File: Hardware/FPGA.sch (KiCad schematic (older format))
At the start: 13 parts, among them U501 W25Q128JVxxM, U502 ICE40UP5K-SG48, U503 Crystal Oscillator, U504 USBLC6-2

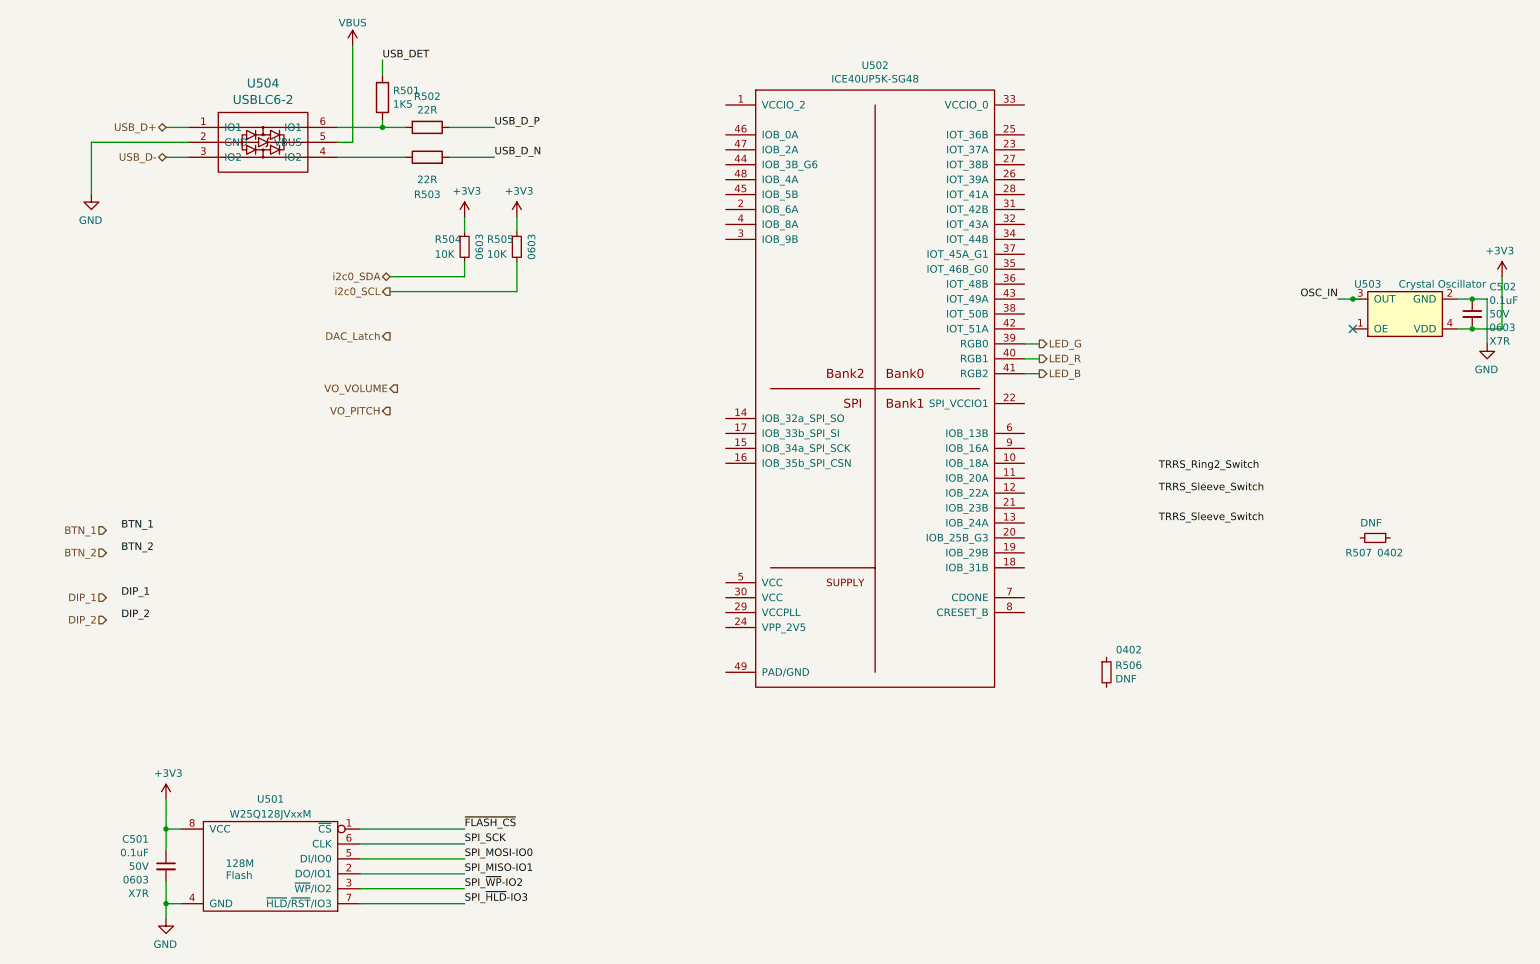
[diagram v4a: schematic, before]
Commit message: Hooking up switches, some more connectivity.
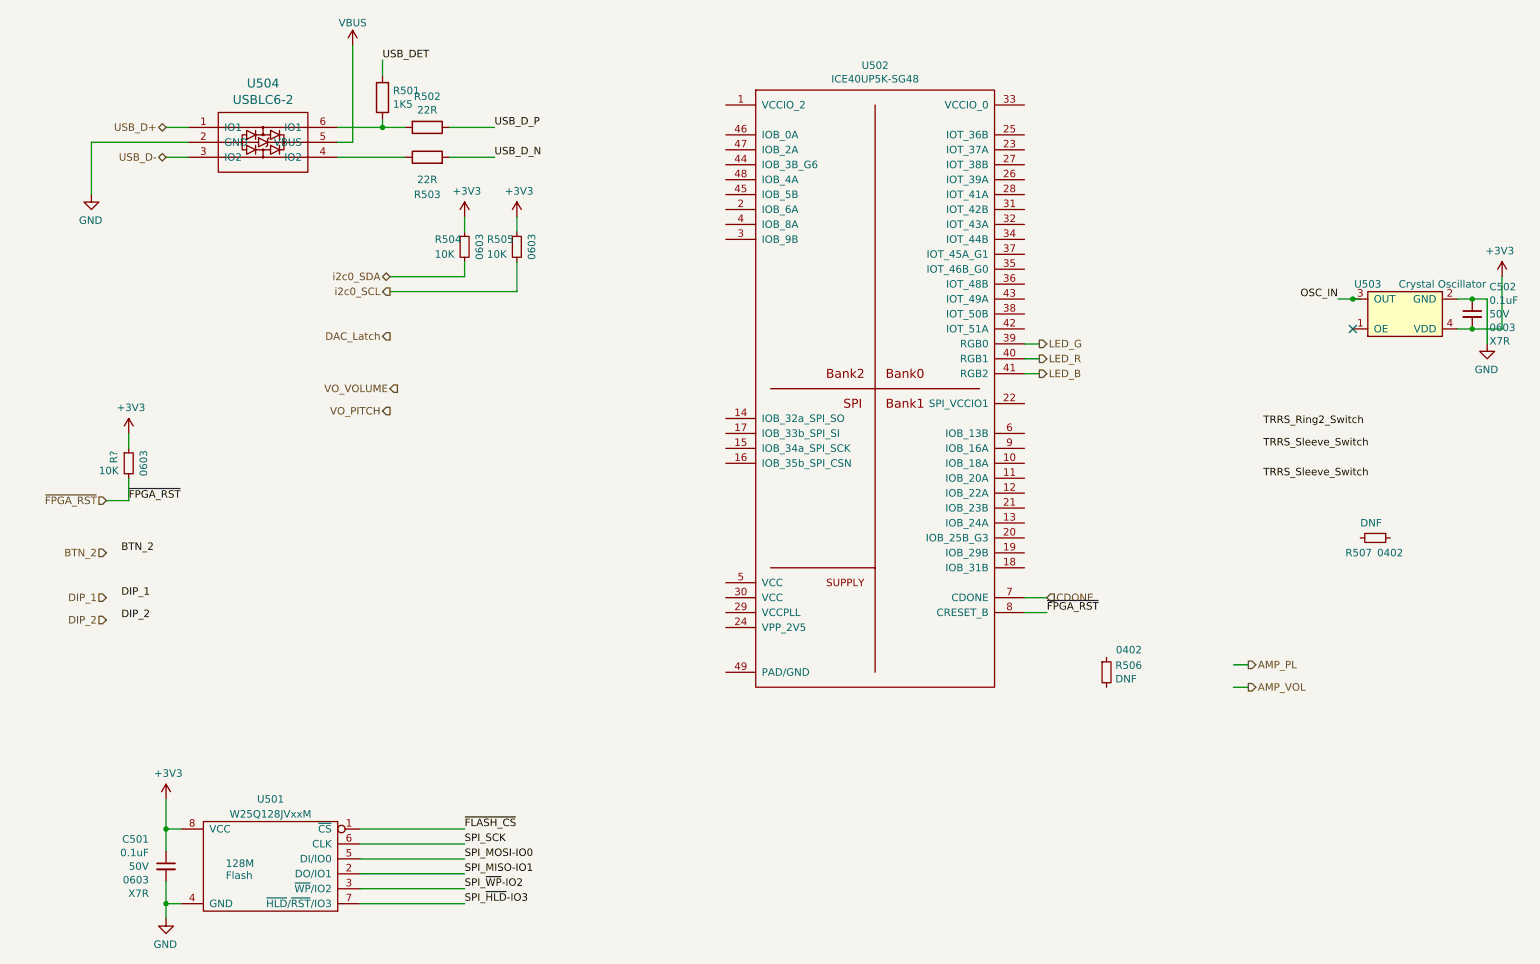
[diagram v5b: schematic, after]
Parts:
- added R?: 10K, Resistor_SMD:R_0603_1608Metric, symbol Device:R_Small
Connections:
- net labels added: AMP_PL, AMP_VOL, CDONE, ~FPGA_RST
- net labels removed: BTN_1
- wire segments 42 -> 49
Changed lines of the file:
@@
 Text HLabel 1300 4250 0    50   Input ~ 0
 BTN_2
-Text HLabel 1300 4100 0    50   Input ~ 0
-BTN_1
+Text HLabel 1300 3900 0    50   Input ~ 0
+~FPGA_RST
 Text HLabel 1300 4700 0    50   Input ~ 0
 DIP_2
@@
 Text Label 1400 4700 0    50   ~ 0
 DIP_2
-Text Label 1400 4100 0    50   ~ 0
-BTN_1
 Text Label 1400 4250 0    50   ~ 0
 BTN_2
@@
 	0    1    1    0
 $EndComp
-Text Label 8350 3700 0    50   ~ 0
+Text Label 9050 3400 0    50   ~ 0
 TRRS_Ring2_Switch
-Text Label 8350 3850 0    50   ~ 0
+Text Label 9050 3550 0    50   ~ 0
 TRRS_Sleeve_Switch
-Text Label 8350 4050 0    50   ~ 0
+Text Label 9050 3750 0    50   ~ 0
 TRRS_Sleeve_Switch
+Text HLabel 8950 5150 2    50   Output ~ 0
+AMP_VOL
+Wire Wire Line
+	8950 5150 8850 5150
+Text HLabel 8950 5000 2    50   Output ~ 0
+AMP_PL
+Wire Wire Line
+	8950 5000 8850 5000
+$Comp
+L Device:R_Small R?
+U 1 1 6165C82A
+P 1450 3650
+AR Path="/611E335F/6165C82A" Ref="R?"  Part="1"
+AR Path="/6165C82A" Ref="R?"  Part="1"
+AR Path="/611E3335/6165C82A" Ref="R?"  Part="1"
+F 0 "R?" V 1350 3650 50  0000 L CNN
+F 1 "10K" H 1250 3600 50  0000 L CNN
+F 2 "Resistor_SMD:R_0603_1608Metric" V 1380 3650 50  0001 C CNN
+F 3 "~" H 1450 3650 50  0001 C CNN
+F 4 "0603" V 1550 3650 50  0000 C CNN "Pkg"
+F 5 "RNCP0603FTD10K0" H 1450 3650 50  0001 C CNN "MPN"
+F 6 "RNCP0603FTD10K0CT-ND" H 1450 3650 50  0001 C CNN "DPN"
+	1    1450 3650
+	1    0    0    -1
+$EndComp
+Wire Wire Line
+	1450 3750 1450 3900
+$Comp
+L power:+3V3 #PWR?
+U 1 1 6165C831
+P 1450 3450
+AR Path="/611E3335/6165C831" Ref="#PWR?"  Part="1"
+AR Path="/6165C831" Ref="#PWR?"  Part="1"
+F 0 "#PWR?" H 1450 3300 50  0001 C CNN
+F 1 "+3V3" H 1465 3623 50  0000 C CNN
+F 2 "" H 1450 3450 50  0001 C CNN
+F 3 "" H 1450 3450 50  0001 C CNN
+	1    1450 3450
+	1    0    0    -1
+$EndComp
+Wire Wire Line
+	1450 3450 1450 3550
+Wire Wire Line
+	1300 3900 1450 3900
+Text Label 1450 3900 0    50   ~ 0
+~FPGA_RST
+Text Label 7600 4650 0    50   ~ 0
+~FPGA_RST
+Wire Wire Line
+	7450 4650 7600 4650
+Text HLabel 7600 4550 2    50   Input ~ 0
+CDONE
+Wire Wire Line
+	7600 4550 7450 4550
 $EndSCHEMATC

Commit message: FPGA wiring.
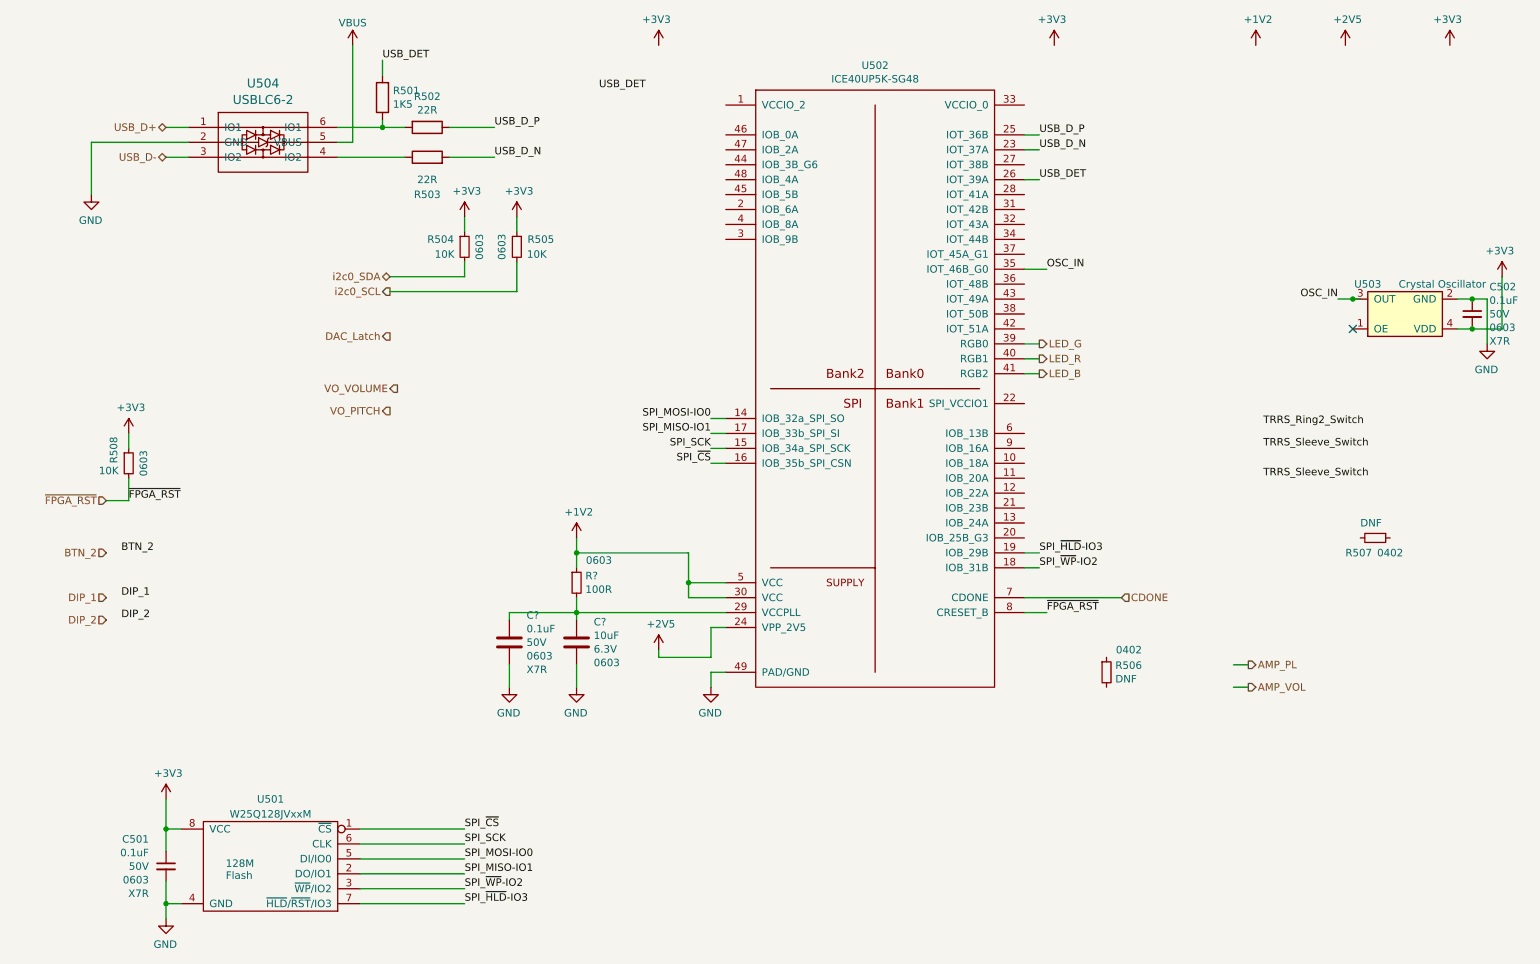
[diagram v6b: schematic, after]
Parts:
- added C?: 10uF, Capacitor_SMD:C_0603_1608Metric, symbol Device:C
- added C?: 0.1uF, Capacitor_SMD:C_0603_1608Metric, symbol Device:C
- added R?: 100R, Resistor_SMD:R_0603_1608Metric, symbol Device:R_Small
- gave numbers to parts that had none: 1
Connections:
- net labels added: +1V2, +2V5, SPI_~CS
- net labels removed: ~FLASH_CS
- wire segments 49 -> 79

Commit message: Wiring up FPGA, picking pins.
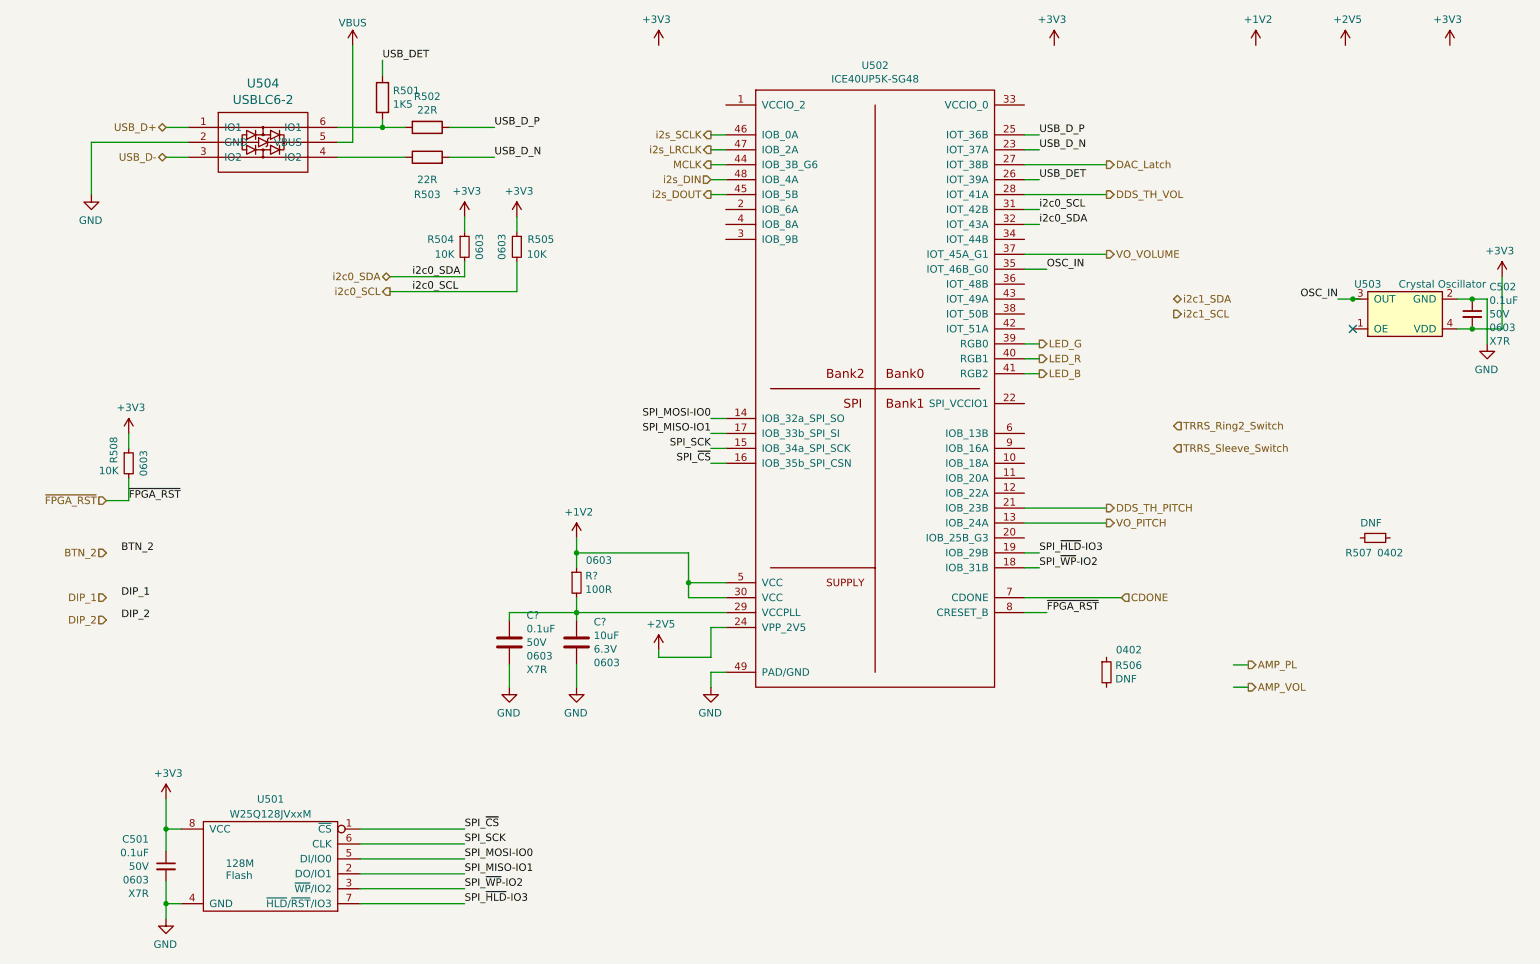
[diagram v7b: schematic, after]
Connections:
- net labels added: DDS_TH_PITCH, DDS_TH_VOL, MCLK, i2c1_SCL, i2c1_SDA, i2s_DIN, i2s_DOUT, i2s_LRCLK, i2s_SCLK
- wire segments 79 -> 91
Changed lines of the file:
@@
 Text HLabel 3200 2500 0    50   Output ~ 0
 i2c0_SCL
-Text HLabel 3200 2800 0    50   Output ~ 0
+Text HLabel 8000 1650 2    50   Output ~ 0
 DAC_Latch
-Text HLabel 3250 3150 0    50   Output ~ 0
+Text HLabel 8000 2250 2    50   Output ~ 0
 VO_VOLUME
-Text HLabel 3200 3300 0    50   Output ~ 0
+Text HLabel 8000 4050 2    50   Output ~ 0
 VO_PITCH
 NoConn ~ 9650 2750
@@
 Wire Wire Line
 	4050 2500 3200 2500
-Text Label 1400 4550 0    50   ~ 0
-DIP_1
-Text Label 1400 4700 0    50   ~ 0
-DIP_2
-Text Label 1400 4250 0    50   ~ 0
-BTN_2
 $Comp
 L Device:R_Small R?
@@
 	0    1    1    0
 $EndComp
-Text Label 9050 3400 0    50   ~ 0
-TRRS_Ring2_Switch
-Text Label 9050 3550 0    50   ~ 0
-TRRS_Sleeve_Switch
-Text Label 9050 3750 0    50   ~ 0
-TRRS_Sleeve_Switch
 Text HLabel 8950 5150 2    50   Output ~ 0
 AMP_VOL
@@
 	-1   0    0    -1
 $EndComp
-Text Label 4600 1150 0    50   ~ 0
-USB_DET
 Text Label 7550 1750 0    50   ~ 0
 USB_DET
@@
 Wire Wire Line
 	7450 4550 8100 4550
+Text Label 1400 4700 0    50   ~ 0
+DIP_2
+Text Label 1400 4550 0    50   ~ 0
+DIP_1
+Text Label 1400 4250 0    50   ~ 0
+BTN_2
+Text HLabel 8450 2650 2    50   Output ~ 0
+i2c1_SCL
+Text HLabel 8450 2550 2    50   BiDi ~ 0
+i2c1_SDA
+Text HLabel 5350 1750 0    50   Input ~ 0
+i2s_DIN
+Text HLabel 5350 1650 0    50   Output ~ 0
+MCLK
+Text HLabel 5350 1850 0    50   Output ~ 0
+i2s_DOUT
+Text HLabel 5350 1550 0    50   Output ~ 0
+i2s_LRCLK
+Text HLabel 5350 1450 0    50   Output ~ 0
+i2s_SCLK
+Wire Wire Line
+	5350 1450 5450 1450
+Wire Wire Line
+	5350 1550 5450 1550
+Wire Wire Line
+	5350 1650 5450 1650
+Wire Wire Line
+	5350 1750 5450 1750
+Wire Wire Line
+	5350 1850 5450 1850
+Text Label 3350 2400 0    50   ~ 0
+i2c0_SDA
+Text Label 3350 2500 0    50   ~ 0
+i2c0_SCL
+Text Label 7550 2050 0    50   ~ 0
+i2c0_SDA
+Text Label 7550 1950 0    50   ~ 0
+i2c0_SCL
+Wire Wire Line
+	7450 1950 7550 1950
+Wire Wire Line
+	7450 2050 7550 2050
+Wire Wire Line
+	8000 4050 7450 4050
+Wire Wire Line
+	8000 2250 7450 2250
+Wire Wire Line
+	8000 1650 7450 1650
+Text HLabel 8000 1850 2    50   Output ~ 0
+DDS_TH_VOL
+Text HLabel 8000 3950 2    50   Output ~ 0
+DDS_TH_PITCH
+Wire Wire Line
+	8000 3950 7450 3950
+Wire Wire Line
+	8000 1850 7450 1850
+Text HLabel 8450 3400 2    50   Input ~ 0
+TRRS_Ring2_Switch
+Text HLabel 8450 3550 2    50   Input ~ 0
+TRRS_Sleeve_Switch
 $EndSCHEMATC
